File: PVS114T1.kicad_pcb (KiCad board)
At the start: 4 copper layers, 53.6 x 45.7 mm, 36 parts, among them J1 61FVXS-RSM1-GAN-TF_LF__SN_, U1 BU90T82-ZE2, U2 LT3473

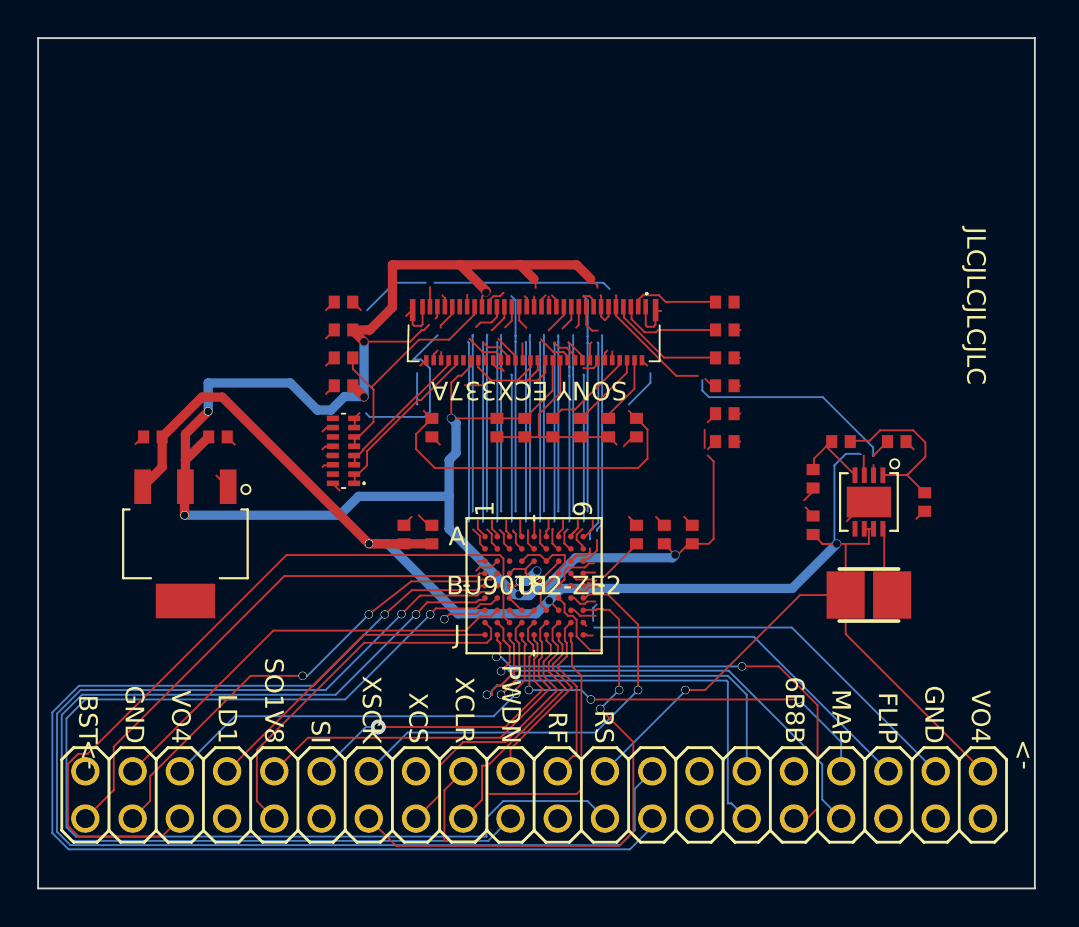
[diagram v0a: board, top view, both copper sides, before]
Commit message: Added a pin header for the config pins 	modified:   PVS114T1.kicad_pcb 	modified:   PVS114T1.kicad_prl 	modified:   PVS114T1.kicad_sch
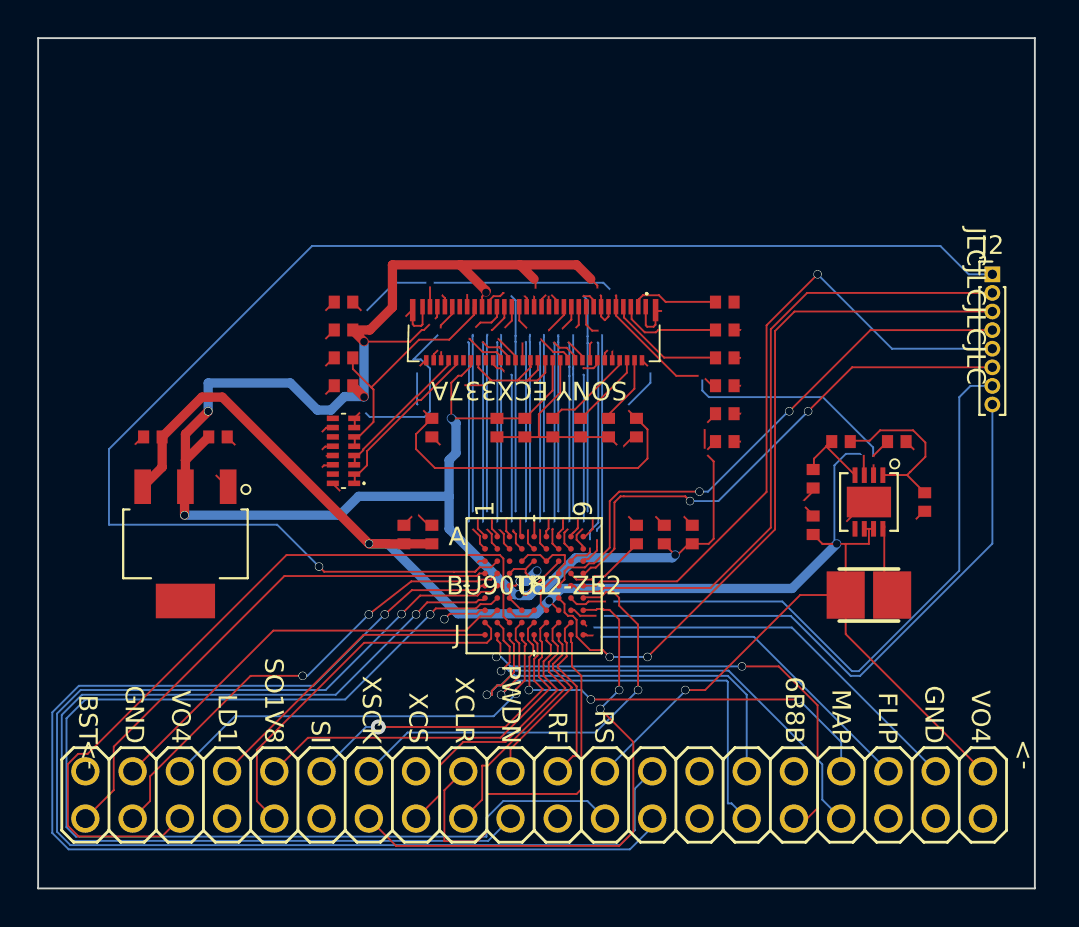
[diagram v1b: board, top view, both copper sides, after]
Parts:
- added J2: Conn_01x08_Male, Connector_PinHeader_1.00mm:PinHeader_1x08_P1.00mm_Vertical, F.Cu at (173.2, 114.3)
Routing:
- net /D_FLIP: track 1.35 -> 78.9 mm, vias 0 -> 1
- net /D_DDRN: track 0.87 -> 36.0 mm, vias 0 -> 1
- net /D_6B8B: track 4.32 -> 39.4 mm, vias 0 -> 2
- net /D_MAP: track 1.78 -> 35.7 mm
- net /D_RS: track 2.95 -> 36.3 mm
- net /D_RF: track 1.73 -> 34.6 mm
- net /D_MODE: track 2.69 -> 30.8 mm, vias 0 -> 2
- net /D_OE: track 0.71 -> 28.3 mm, vias 0 -> 2
